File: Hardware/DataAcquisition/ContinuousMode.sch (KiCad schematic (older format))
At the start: 8 parts, among them Q10 Q_NJFET_DGS, Q6 Q_NJFET_DGS

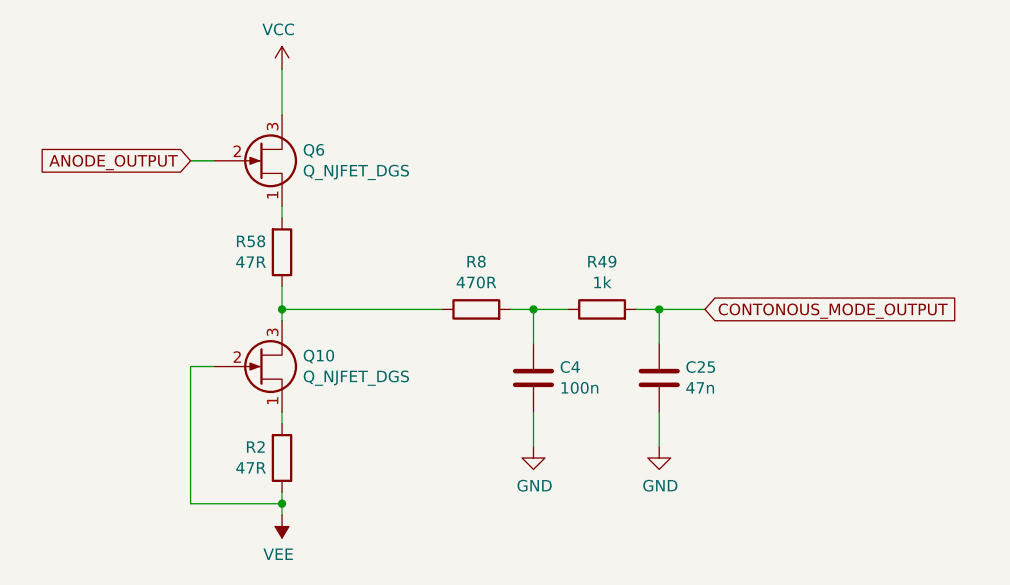
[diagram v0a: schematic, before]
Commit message: split (previousle one) pcb project to three separate pcbs
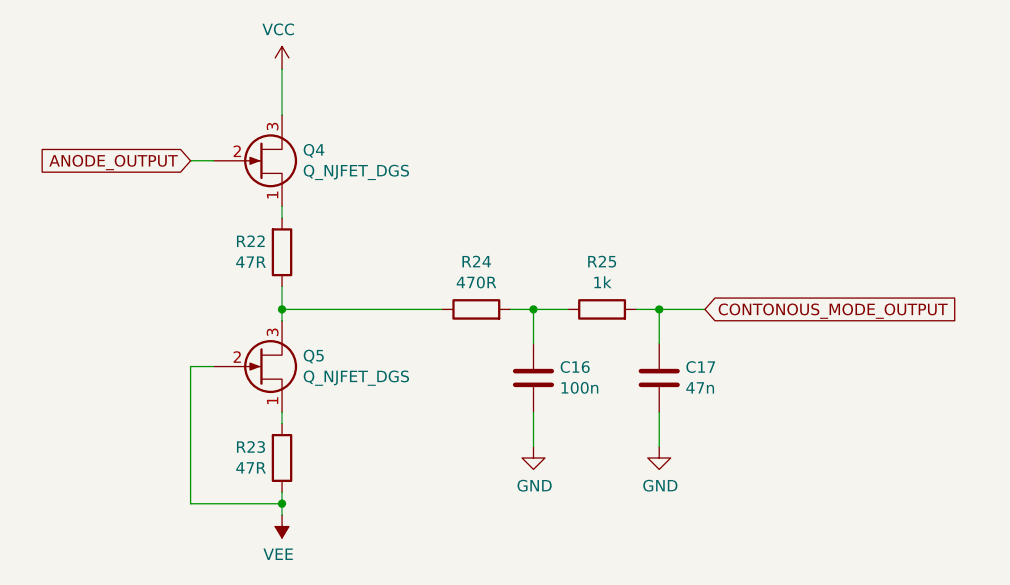
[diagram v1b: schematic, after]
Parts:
- renumbered C4 to C16, C25 to C17, Q6 to Q4, Q10 to Q5, R58 to R22, R2 to R23, R8 to R24, R49 to R25
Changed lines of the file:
@@
 $Descr A4 11693 8268
 encoding utf-8
-Sheet 6 7
+Sheet 6 5
 Title ""
 Date ""
@@
 P 4100 3800
 AR Path="/5EFA52FA/5EE68A9A" Ref="R?"  Part="1"
-AR Path="/5EE61922/5EE68A9A" Ref="R49"  Part="1"
-F 0 "R49" V 4307 3800 50  0000 C CNN
+AR Path="/5EE61922/5EE68A9A" Ref="R25"  Part="1"
+F 0 "R25" V 4307 3800 50  0000 C CNN
 F 1 "1k" V 4216 3800 50  0000 C CNN
 F 2 "Resistor_SMD:R_0805_2012Metric_Pad1.15x1.40mm_HandSolder" V 4030 3800 50  0001 C CNN
@@
 P 4350 4100
 AR Path="/5EFA52FA/5EE68AB2" Ref="C?"  Part="1"
-AR Path="/5EE61922/5EE68AB2" Ref="C25"  Part="1"
-F 0 "C25" H 4465 4146 50  0000 L CNN
+AR Path="/5EE61922/5EE68AB2" Ref="C17"  Part="1"
+F 0 "C17" H 4465 4146 50  0000 L CNN
 F 1 "47n" H 4465 4055 50  0000 L CNN
 F 2 "Capacitor_SMD:C_0805_2012Metric_Pad1.15x1.40mm_HandSolder" H 4388 3950 50  0001 C CNN
@@
 AR Path="/5EDA53F3/5EE68B12" Ref="#PWR?"  Part="1"
 AR Path="/5EFA52FA/5EE68B12" Ref="#PWR?"  Part="1"
-AR Path="/5EE61922/5EE68B12" Ref="#PWR038"  Part="1"
-F 0 "#PWR038" H 4350 4150 50  0001 C CNN
+AR Path="/5EE61922/5EE68B12" Ref="#PWR037"  Part="1"
+F 0 "#PWR037" H 4350 4150 50  0001 C CNN
 F 1 "GND" H 4355 4227 50  0000 C CNN
 F 2 "" H 4350 4400 50  0001 C CNN
@@
 AR Path="/5EFA52FA/5EF7B706" Ref="#PWR?"  Part="1"
 AR Path="/5EE9D63B/5EF7B706" Ref="#PWR?"  Part="1"
-AR Path="/5EE61922/5EF7B706" Ref="#PWR068"  Part="1"
-F 0 "#PWR068" H 2700 2600 50  0001 C CNN
+AR Path="/5EE61922/5EF7B706" Ref="#PWR034"  Part="1"
+F 0 "#PWR034" H 2700 2600 50  0001 C CNN
 F 1 "VCC" H 2715 2923 50  0000 C CNN
 F 2 "" H 2700 2750 50  0001 C CNN
@@
 P 2600 3150
 AR Path="/5EE9D63B/5EF7B712" Ref="Q?"  Part="1"
-AR Path="/5EE61922/5EF7B712" Ref="Q6"  Part="1"
-F 0 "Q6" H 2791 3104 50  0000 L CNN
+AR Path="/5EE61922/5EF7B712" Ref="Q4"  Part="1"
+F 0 "Q4" H 2791 3104 50  0000 L CNN
 F 1 "Q_NJFET_DGS" H 2791 3195 50  0000 L CNN
 F 2 "Package_TO_SOT_SMD:SC-59" H 2800 3250 50  0001 C CNN
@@
 P 2600 4050
 AR Path="/5EE9D63B/5F145708" Ref="Q?"  Part="1"
-AR Path="/5EE61922/5F145708" Ref="Q10"  Part="1"
-F 0 "Q10" H 2791 4004 50  0000 L CNN
+AR Path="/5EE61922/5F145708" Ref="Q5"  Part="1"
+F 0 "Q5" H 2791 4004 50  0000 L CNN
 F 1 "Q_NJFET_DGS" H 2791 4095 50  0000 L CNN
 F 2 "Package_TO_SOT_SMD:SC-59" H 2800 4150 50  0001 C CNN
@@
 AR Path="/5EFA52FA/5EF7B70C" Ref="R?"  Part="1"
 AR Path="/5EE9D63B/5EF7B70C" Ref="R?"  Part="1"
-AR Path="/5EE61922/5EF7B70C" Ref="R58"  Part="1"
-F 0 "R58" H 2631 3504 50  0000 R CNN
+AR Path="/5EE61922/5EF7B70C" Ref="R22"  Part="1"
+F 0 "R22" H 2631 3504 50  0000 R CNN
 F 1 "47R" H 2631 3595 50  0000 R CNN
 F 2 "Resistor_SMD:R_0805_2012Metric_Pad1.15x1.40mm_HandSolder" V 2630 3550 50  0001 C CNN
@@
 AR Path="/5EFA52FA/5F1475A6" Ref="R?"  Part="1"
 AR Path="/5EE9D63B/5F1475A6" Ref="R?"  Part="1"
-AR Path="/5EE61922/5F1475A6" Ref="R2"  Part="1"
-F 0 "R2" H 2631 4404 50  0000 R CNN
+AR Path="/5EE61922/5F1475A6" Ref="R23"  Part="1"
+F 0 "R23" H 2631 4404 50  0000 R CNN
 F 1 "47R" H 2631 4495 50  0000 R CNN
 F 2 "Resistor_SMD:R_0805_2012Metric_Pad1.15x1.40mm_HandSolder" V 2630 4450 50  0001 C CNN
@@
 P 3550 3800
 AR Path="/5EFA52FA/5F14C90F" Ref="R?"  Part="1"
-AR Path="/5EE61922/5F14C90F" Ref="R8"  Part="1"
-F 0 "R8" V 3757 3800 50  0000 C CNN
+AR Path="/5EE61922/5F14C90F" Ref="R24"  Part="1"
+F 0 "R24" V 3757 3800 50  0000 C CNN
 F 1 "470R" V 3666 3800 50  0000 C CNN
 F 2 "Resistor_SMD:R_0805_2012Metric_Pad1.15x1.40mm_HandSolder" V 3480 3800 50  0001 C CNN
@@
 P 3800 4100
 AR Path="/5EFA52FA/5F14C915" Ref="C?"  Part="1"
-AR Path="/5EE61922/5F14C915" Ref="C4"  Part="1"
-F 0 "C4" H 3915 4146 50  0000 L CNN
+AR Path="/5EE61922/5F14C915" Ref="C16"  Part="1"
+F 0 "C16" H 3915 4146 50  0000 L CNN
 F 1 "100n" H 3915 4055 50  0000 L CNN
 F 2 "Capacitor_SMD:C_0805_2012Metric_Pad1.15x1.40mm_HandSolder" H 3838 3950 50  0001 C CNN
